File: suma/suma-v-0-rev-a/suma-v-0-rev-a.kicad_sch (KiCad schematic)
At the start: 0 parts

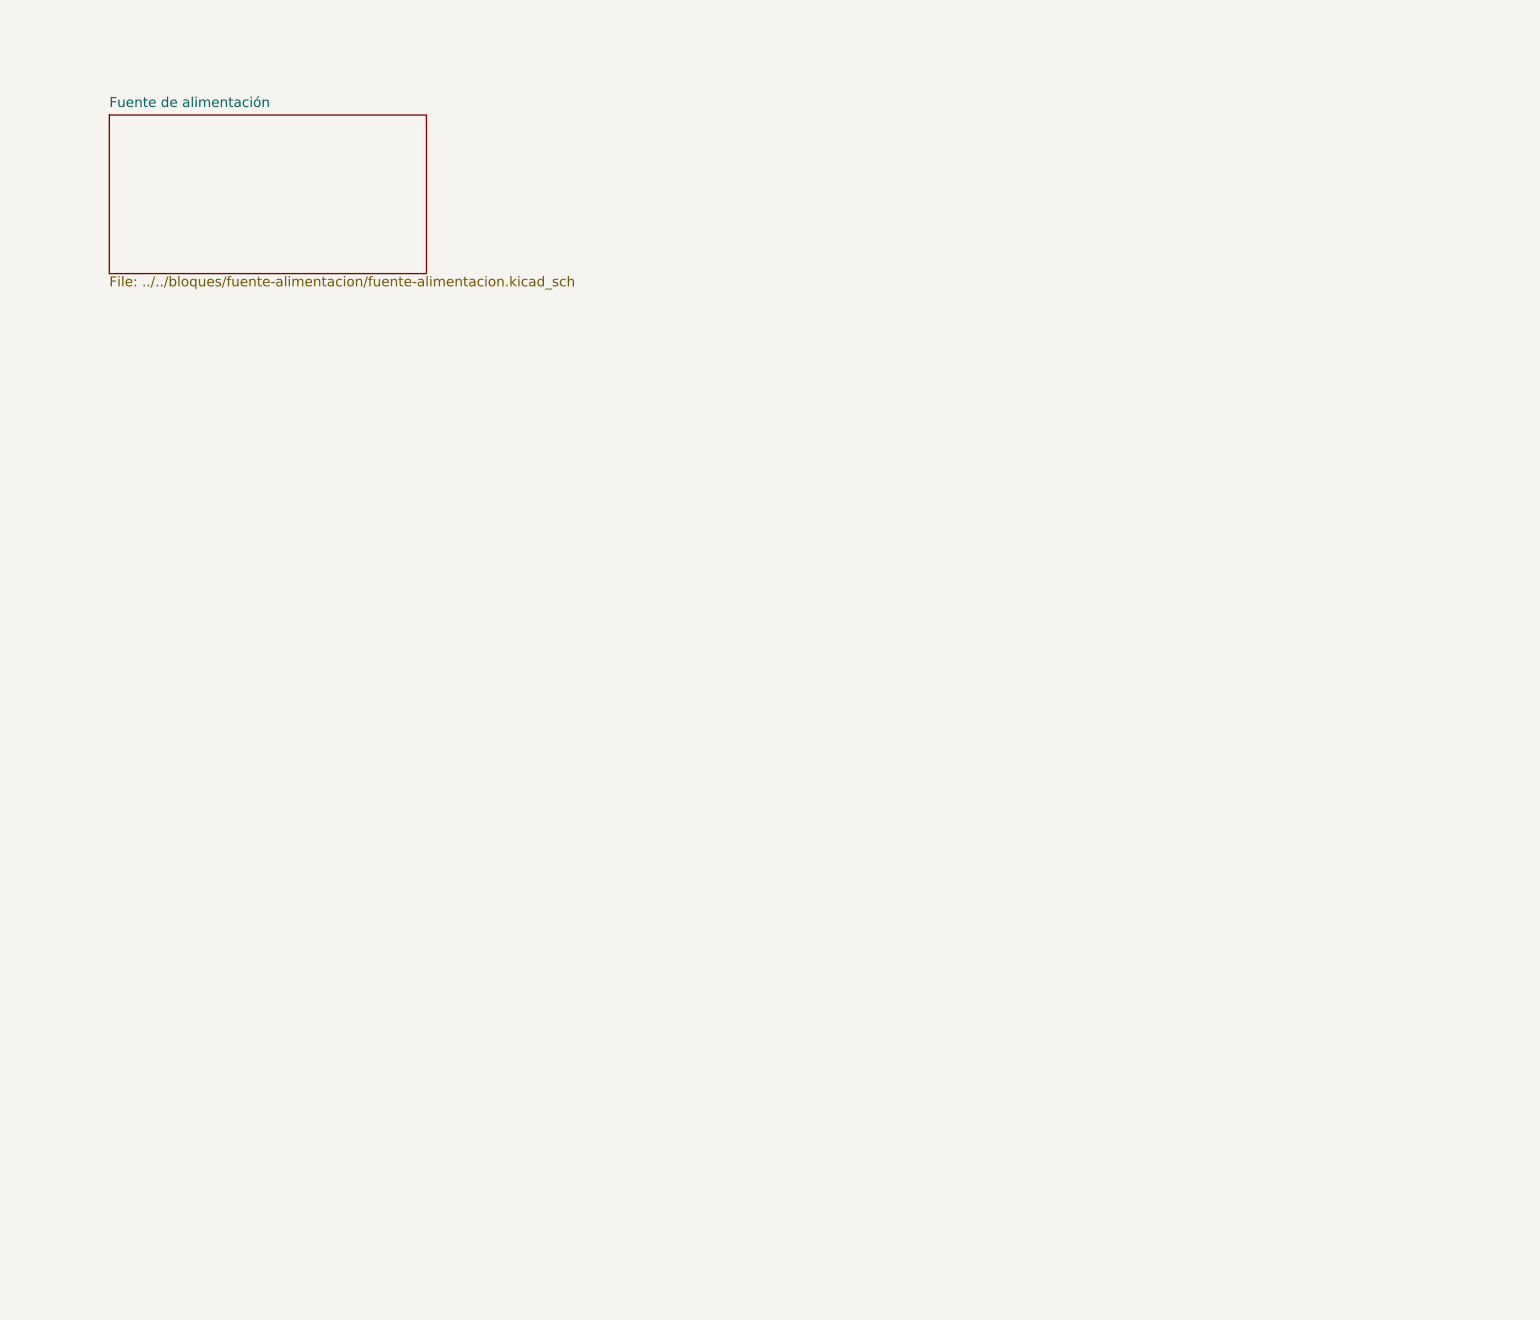
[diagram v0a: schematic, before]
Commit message: agregar suma-v-0-rev-a esquematico
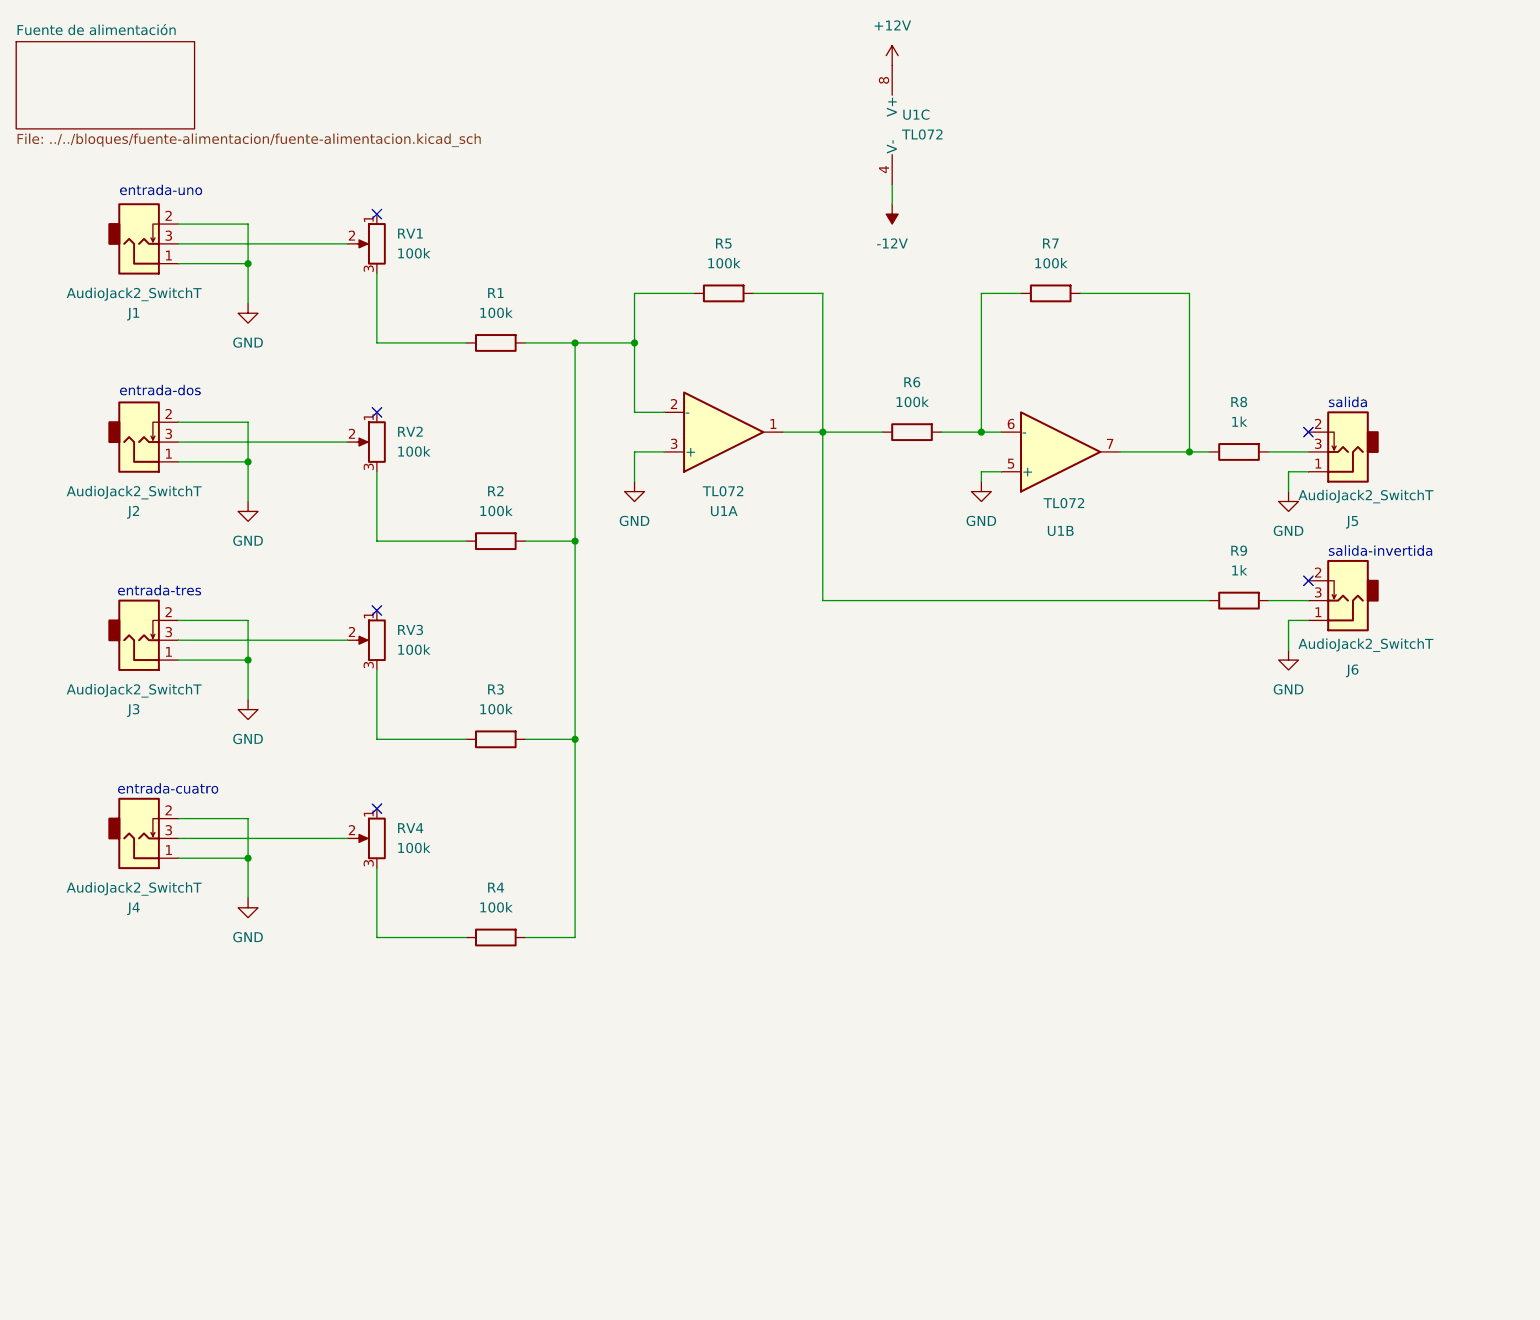
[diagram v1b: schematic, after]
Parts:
- added J1, J2, J3, J4, J5, J6: AudioJack2_SwitchT, symbol Connector_Audio:AudioJack2_SwitchT
- added R1, R2, R3, R4, R5, R6, R7: 100k, symbol Device:R
- added R8, R9: 1k, symbol Device:R
- added RV1, RV2, RV3, RV4: 100k, symbol Device:R_Potentiometer
- added U1: TL072, symbol Amplifier_Operational:TL072
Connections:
- new net: J2.3, RV2.2
- new net: R3.1, RV3.3
- new net: R1.2, R2.2, R3.2, R4.2, R5.1, U1.2 (-)
- new net: J5.3, R8.2
- new net: R2.1, RV2.3
- new net: R4.1, RV4.3
- new net: J3.3, RV3.2
- new net: R5.2, R6.1, R9.1, U1.1
- new net: J6.3, R9.2
- new net: R7.2, R8.1, U1.7
- new net: J4.3, RV4.2
- new net: R6.2, R7.1, U1.6 (-)
- new net: R1.1, RV1.3
- new net: J1.3, RV1.2
- new net +12V: U1.8 (V+)
- new net -12V: U1.4 (V-)
- new net GND: J1.1, J1.2, J2.1, J2.2, J3.1, J3.2, J4.1, J4.2, J5.1, J6.1, U1.3 (+), U1.5 (+)
- no-connect marks 0 -> 6
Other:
- note added: "entrada-cuatro"
- note added: "entrada-dos"
- note added: "entrada-tres"
- note added: "entrada-uno"
- note added: "salida"
- note added: "salida-invertida"

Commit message: agregar suma
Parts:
- J1, J2, J3, J4, J5, J6: footprint (none) -> suma-v-0-rev-a:Jack_3.5mm_QingPu_WQP-PJ398SM_Vertical
- R1, R2, R3, R4, R5, R6, R7, R8, R9: footprint (none) -> suma-v-0-rev-a:R0805
- RV1, RV2, RV3, RV4: footprint (none) -> suma-v-0-rev-a:POT_TH_Alps_RK09K_Single_Vertical
- U1: footprint (none) -> suma-v-0-rev-a:SOIC-8_L4.9-W3.9-P1.27-LS6.0-BL
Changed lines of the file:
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@@
 			)
 		)
-		(property "Footprint" ""
+		(property "Footprint" "suma-v-0-rev-a:Jack_3.5mm_QingPu_WQP-PJ398SM_Vertical"
 			(at 29.21 67.31 0)
 			(hide yes)
@@
 			)
 		)
-		(property "Footprint" ""
+		(property "Footprint" "suma-v-0-rev-a:R0805"
 			(at 74.93 103.632 90)
 			(hide yes)
@@
 			)
 		)
-		(property "Footprint" ""
+		(property "Footprint" "suma-v-0-rev-a:Jack_3.5mm_QingPu_WQP-PJ398SM_Vertical"
 			(at 184.15 68.58 0)
 			(hide yes)
@@
 			)
 		)
-		(property "Footprint" ""
+		(property "Footprint" "suma-v-0-rev-a:POT_TH_Alps_RK09K_Single_Vertical"
 			(at 59.69 67.31 0)
 			(hide yes)
@@
 			)
 		)
-		(property "Footprint" ""
+		(property "Footprint" "suma-v-0-rev-a:R0805"
 			(at 74.93 129.032 90)
 			(hide yes)
@@
 			)
 		)
-		(property "Footprint" ""
+		(property "Footprint" "suma-v-0-rev-a:POT_TH_Alps_RK09K_Single_Vertical"
 			(at 59.69 92.71 0)
 			(hide yes)
@@
 			)
 		)
-		(property "Footprint" ""
+		(property "Footprint" "suma-v-0-rev-a:R0805"
 			(at 170.18 85.852 90)
 			(hide yes)
@@
 			)
 		)
-		(property "Footprint" ""
+		(property "Footprint" "suma-v-0-rev-a:SOIC-8_L4.9-W3.9-P1.27-LS6.0-BL"
 			(at 128.27 26.67 0)
 			(hide yes)
@@
 			)
 		)
-		(property "Footprint" ""
+		(property "Footprint" "suma-v-0-rev-a:R0805"
 			(at 170.18 66.802 90)
 			(hide yes)
@@
 			)
 		)
-		(property "Footprint" ""
+		(property "Footprint" "suma-v-0-rev-a:POT_TH_Alps_RK09K_Single_Vertical"
 			(at 59.69 118.11 0)
 			(hide yes)
@@
 			)
 		)
-		(property "Footprint" ""
+		(property "Footprint" "suma-v-0-rev-a:R0805"
 			(at 74.93 78.232 90)
 			(hide yes)
@@
 			)
 		)
-		(property "Footprint" ""
+		(property "Footprint" "suma-v-0-rev-a:SOIC-8_L4.9-W3.9-P1.27-LS6.0-BL"
 			(at 104.14 66.04 0)
 			(hide yes)
@@
 			)
 		)
-		(property "Footprint" ""
+		(property "Footprint" "suma-v-0-rev-a:Jack_3.5mm_QingPu_WQP-PJ398SM_Vertical"
 			(at 29.21 118.11 0)
 			(hide yes)
@@
 			)
 		)
-		(property "Footprint" ""
+		(property "Footprint" "suma-v-0-rev-a:R0805"
 			(at 128.27 64.262 90)
 			(hide yes)
@@
 			)
 		)
-		(property "Footprint" ""
+		(property "Footprint" "suma-v-0-rev-a:R0805"
 			(at 74.93 52.832 90)
 			(hide yes)
@@
 			)
 		)
-		(property "Footprint" ""
+		(property "Footprint" "suma-v-0-rev-a:POT_TH_Alps_RK09K_Single_Vertical"
 			(at 59.69 41.91 0)
 			(hide yes)
@@
 			)
 		)
-		(property "Footprint" ""
+		(property "Footprint" "suma-v-0-rev-a:Jack_3.5mm_QingPu_WQP-PJ398SM_Vertical"
 			(at 29.21 92.71 0)
 			(hide yes)
@@
 			)
 		)
-		(property "Footprint" ""
+		(property "Footprint" "suma-v-0-rev-a:Jack_3.5mm_QingPu_WQP-PJ398SM_Vertical"
 			(at 184.15 87.63 0)
 			(hide yes)
@@
 			)
 		)
-		(property "Footprint" ""
+		(property "Footprint" "suma-v-0-rev-a:SOIC-8_L4.9-W3.9-P1.27-LS6.0-BL"
 			(at 147.32 68.58 0)
 			(hide yes)
@@
 			)
 		)
-		(property "Footprint" ""
+		(property "Footprint" "suma-v-0-rev-a:R0805"
 			(at 104.14 46.482 90)
 			(hide yes)
@@
 			)
 		)
-		(property "Footprint" ""
+		(property "Footprint" "suma-v-0-rev-a:R0805"
 			(at 146.05 46.482 90)
 			(hide yes)
@@
 			)
 		)
-		(property "Footprint" ""
+		(property "Footprint" "suma-v-0-rev-a:Jack_3.5mm_QingPu_WQP-PJ398SM_Vertical"
 			(at 29.21 41.91 0)
 			(hide yes)

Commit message: agregar borrador de pcb
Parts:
- removed J4: AudioJack2_SwitchT, suma-v-0-rev-a:Jack_3.5mm_QingPu_WQP-PJ398SM_Vertical, symbol Connector_Audio:AudioJack2_SwitchT
- removed R4: 100k, suma-v-0-rev-a:R0805, symbol Device:R
- removed RV4: 100k, suma-v-0-rev-a:POT_TH_Alps_RK09K_Single_Vertical, symbol Device:R_Potentiometer
- renumbered J5 to J4, J6 to J5, R5 to R4, R6 to R5, R7 to R6, R8 to R7, R9 to R8
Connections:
- no-connect marks 6 -> 5
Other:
- note removed: "entrada-cuatro"

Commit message: agregar blocks
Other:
- sheet Fuente de alimentación: file ../../bloques/fuente-alimentacion/fuente-alimentacion.kicad_sch -> fuente-alimentacion.kicad_sch
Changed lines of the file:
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@@
 			)
 		)
-		(property "Sheetfile" "../../bloques/fuente-alimentacion/fuente-alimentacion.kicad_sch"
+		(property "Sheetfile" "fuente-alimentacion.kicad_sch"
 			(at 13.462 27.7626 0)
 			(show_name no)

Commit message: avanzar en lcsc, huellas, stock
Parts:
- R1, R2, R3, R4, R5, R6: LCSC (none) -> C25611
- R7, R8: LCSC (none) -> C2907232
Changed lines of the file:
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@@
+			)
+		)
+		(property "LCSC" "C25611"
+			(at 74.93 105.41 0)
+			(hide yes)
+			(show_name no)
+			(do_not_autoplace no)
+			(effects
+				(font
+					(size 1.27 1.27)
+				)
 			)
 		)
@@
 			)
 		)
+		(property "LCSC" "C2907232"
+			(at 170.18 87.63 0)
+			(hide yes)
+			(show_name no)
+			(do_not_autoplace no)
+			(effects
+				(font
+					(size 1.27 1.27)
+				)
+			)
+		)
 		(pin "1"
 		)
@@
 			)
 		)
+		(property "LCSC" "C2907232"
+			(at 170.18 68.58 0)
+			(hide yes)
+			(show_name no)
+			(do_not_autoplace no)
+			(effects
+				(font
+					(size 1.27 1.27)
+				)
+			)
+		)
 		(pin "1"
 		)
@@
 			)
 		)
+		(property "LCSC" "C25611"
+			(at 74.93 80.01 0)
+			(hide yes)
+			(show_name no)
+			(do_not_autoplace no)
+			(effects
+				(font
+					(size 1.27 1.27)
+				)
+			)
+		)
 		(pin "1"
 		)
@@
 			)
 		)
+		(property "LCSC" "C25611"
+			(at 128.27 66.04 0)
+			(hide yes)
+			(show_name no)
+			(do_not_autoplace no)
+			(effects
+				(font
+					(size 1.27 1.27)
+				)
+			)
+		)
 		(pin "1"
 		)
@@
 			)
 		)
+		(property "LCSC" "C25611"
+			(at 74.93 54.61 0)
+			(hide yes)
+			(show_name no)
+			(do_not_autoplace no)
+			(effects
+				(font
+					(size 1.27 1.27)
+				)
+			)
+		)
 		(pin "1"
 		)
@@
 			)
 		)
+		(property "LCSC" "C25611"
+			(at 104.14 48.26 0)
+			(hide yes)
+			(show_name no)
+			(do_not_autoplace no)
+			(effects
+				(font
+					(size 1.27 1.27)
+				)
+			)
+		)
 		(pin "1"
 		)
@@
 			(at 146.05 48.26 0)
 			(hide yes)
+			(show_name no)
+			(do_not_autoplace no)
+			(effects
+				(font
+					(size 1.27 1.27)
+				)
+			)
+		)
+		(property "LCSC" "C25611"
+			(at 146.05 48.26 0)
+			(hide yes)

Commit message: agregar nueva pcb
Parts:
- removed RV1, RV2, RV3: 100k, suma-v-0-rev-a:POT_TH_Alps_RK09K_Single_Vertical, symbol Device:R_Potentiometer
- added C1, C2: 100n, suma-v-0-rev-a:C0805, symbol suma-v-0-rev-a:C
- added D1, D2: 1N5817W, suma-v-0-rev-a:SOD-123FL_L2.8-W1.8-LS3.7-R-RD, symbol suma-v-0-rev-a:D_Schottky
- added J4: Conn_02x05_Odd_Even, suma-v-0-rev-a:IDC-Header_2x05_P2.54mm_Vertical, symbol suma-v-0-rev-a:Conn_02x05_Odd_Even
- added RV1, RV2, RV3: A100k, suma-v-0-rev-a:POT_TH_Alps_RK09K_Single_Vertical, symbol suma-v-0-rev-a:R_Potentiometer
- J1, J2, J3: symbol Connector_Audio:AudioJack2_SwitchT -> suma-v-0-rev-a:AudioJack2_SwitchT
- J5: renamed from J4; symbol Connector_Audio:AudioJack2_SwitchT -> suma-v-0-rev-a:AudioJack2_SwitchT
- J6: renamed from J5; symbol Connector_Audio:AudioJack2_SwitchT -> suma-v-0-rev-a:AudioJack2_SwitchT
- R1, R2, R3, R4, R5, R6, R7, R8: symbol Device:R -> suma-v-0-rev-a:R
- U1: symbol Amplifier_Operational:TL072 -> suma-v-0-rev-a:TL072; LCSC (none) -> C6962
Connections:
- net +12V: now also C1.2, D1.1 (K)
- net -12V: now also C2.2, D2.2 (A)
- net GND: now also C1.1, C2.1, J4.3 (Pin_3), J4.4 (Pin_4), J4.5 (Pin_5), J4.6 (Pin_6), J4.7 (Pin_7), J4.8 (Pin_8), RV1.1, RV2.1, RV3.1
- net at J2.3: now also RV2.3
- net at R3.1: now also RV3.2
- net at R2.1: now also RV2.2
- net at J3.3: now also RV3.3
- net at R1.1: now also RV1.2
- net at J1.3: now also RV1.3
- new net: D2.1 (K), J4.1 (Pin_1), J4.2 (Pin_2)
- new net: D1.2 (A), J4.10 (Pin_10), J4.9 (Pin_9)
- no-connect marks 5 -> 2
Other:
- removed sheet Fuente de alimentación
- title: (none) -> suma-v-0
- moved on the sheet: J1, J2, J3, J5, J6, R1, R2, R3, R4, R5, R6, R7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
